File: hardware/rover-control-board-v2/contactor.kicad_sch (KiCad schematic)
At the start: 9 parts, among them Q27 Q_NMOS_DGS

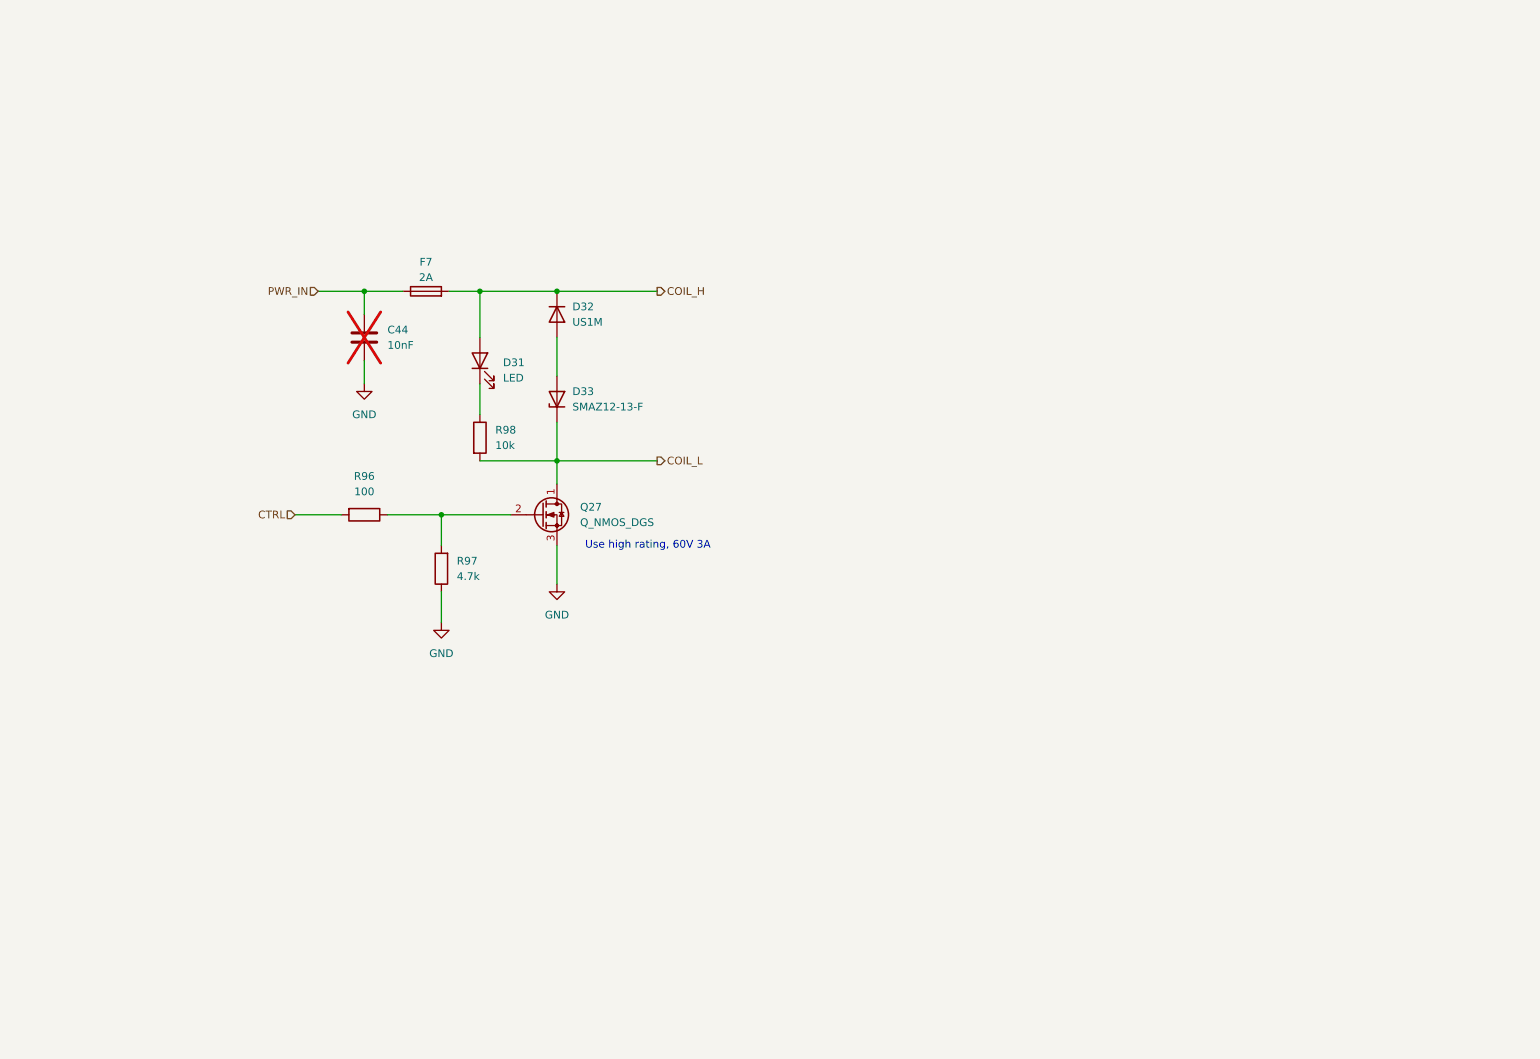
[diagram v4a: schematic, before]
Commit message: footprints and BOM additions
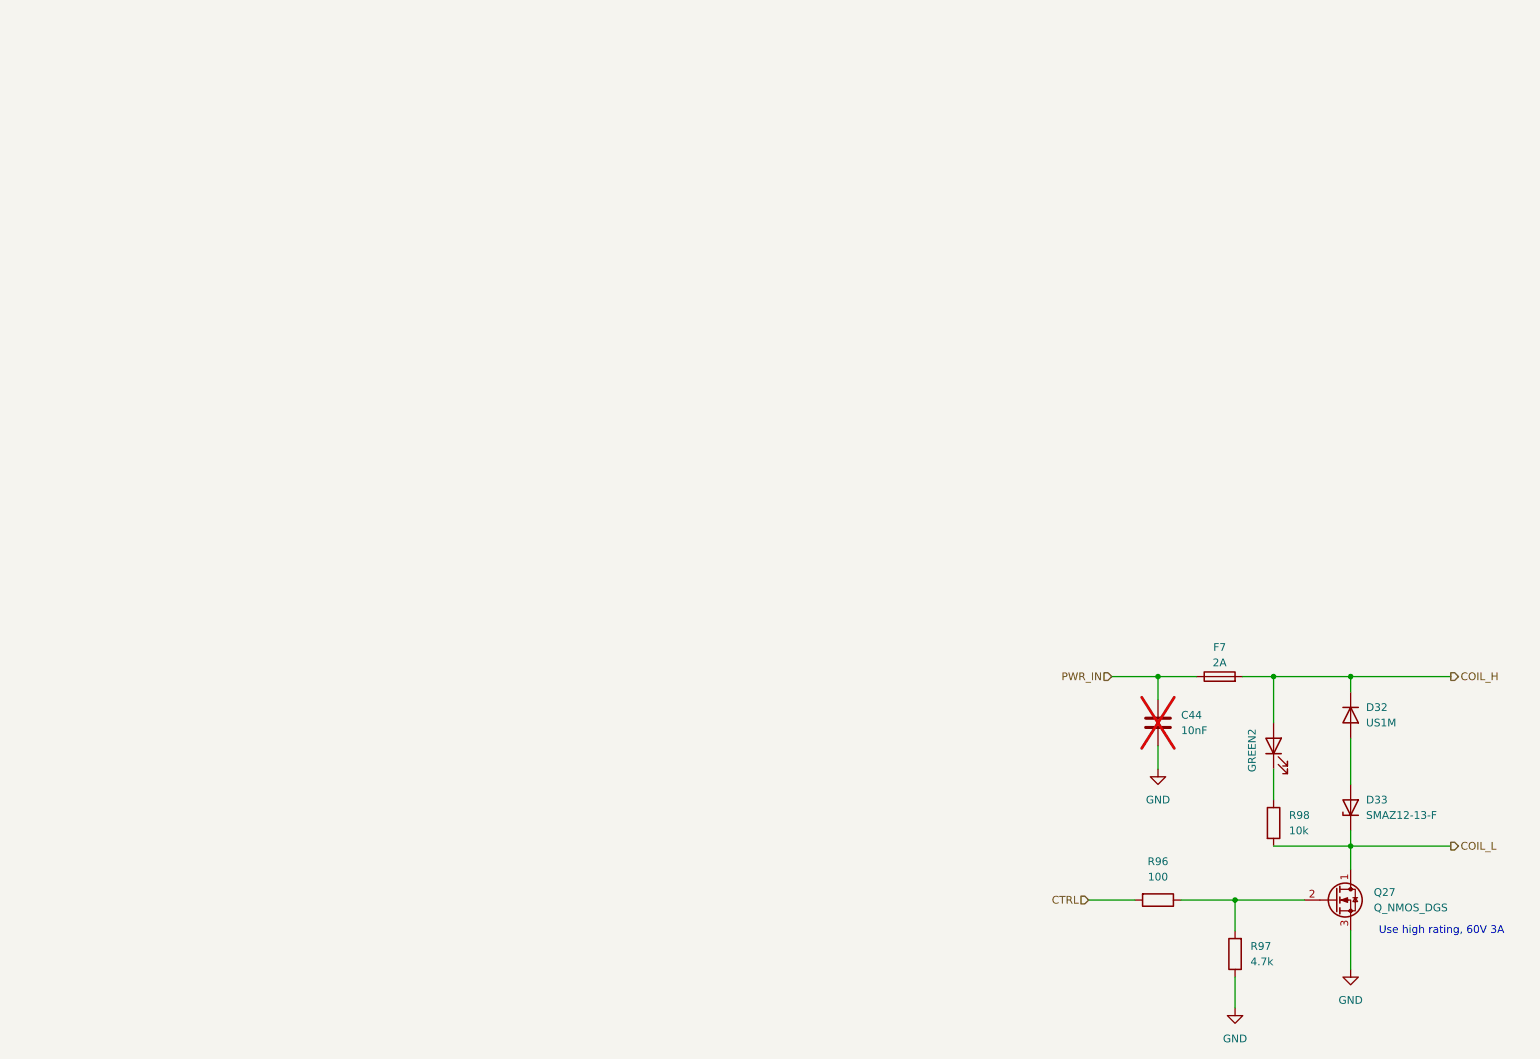
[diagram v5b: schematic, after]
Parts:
- removed D31: LED, symbol Device:LED
- added GREEN2: 350-599, LED_SMD:LED_0805_2012Metric, symbol Device:LED
- C44: footprint (none) -> Capacitor_SMD:C_0603_1608Metric
- D32: digikey_part_num (none) -> 4878-US1MCT-ND
- D33: footprint (none) -> Diode_SMD:D_SMA; digikey_part_num (none) -> SMAZ12-FDICT-ND
- R96, R97, R98: footprint (none) -> Resistor_SMD:R_0603_1608Metric
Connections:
- net COIL_H: now also GREEN2.2 (A)
- net at R98.1: now also GREEN2.1 (K)
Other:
- title: (none) -> Rover Control Board
- moved on the sheet: C44, D32, D33, F7, Q27, R96, R97, R98

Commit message: BOM
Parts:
- removed Q27: Q_NMOS_DGS, symbol Transistor_FET:Q_NMOS_DGS
- added Q3: NMOS_GDS, Package_TO_SOT_SMD:SOT-223, symbol Transistor_FET_Other:Q_NMOS_Depletion_GDS
- F7: footprint (none) -> Fuse:Fuse_2920_7451Metric_Pad2.10x5.45mm_HandSolder; digikey_part_num (none) -> 5923-0ZCF0100AF2ACT-ND
- GREEN2: digikey_part_num (none) -> 350-5991180147FCT-ND
- R96: value 100 -> 100R; digikey_part_num (none) -> 541-100HCT-ND
- R97: digikey_part_num (none) -> 311-4.70KHRCT-ND
- R98: digikey_part_num (none) -> 311-10.0KHRCT-ND
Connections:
- net COIL_L: now also Q3.2 (D)
- net GND: now also Q3.3 (S)
- net at R96.1, R97.2: now also Q3.1 (G)
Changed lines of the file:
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@@
+			)
+		)
+		(property "digikey_part_num" "350-5991180147FCT-ND"
+			(at 207.01 120.65 0)
+			(hide yes)
+			(show_name no)
+			(do_not_autoplace no)
+			(effects
+				(font
+					(size 1.27 1.27)
+				)
 			)
 		)
@@
 	)
 	(symbol
-		(lib_id "Transistor_FET:Q_NMOS_DGS")
+		(lib_id "Transistor_FET_Other:Q_NMOS_Depletion_GDS")
 		(at 217.17 146.05 0)
 		(unit 1)
@@
 		(dnp no)
 		(fields_autoplaced yes)
-		(property "Reference" "Q27"
+		(property "Reference" "Q3"
 			(at 223.52 144.7799 0)
 			(show_name no)
@@
 			)
 		)
-		(property "Value" "Q_NMOS_DGS"
+		(property "Value" "NMOS_GDS"
 			(at 223.52 147.3199 0)
 			(show_name no)
@@
 			)
 		)
-		(property "Footprint" ""
-			(at 222.25 143.51 0)
-			(hide yes)
-			(show_name no)
-			(do_not_autoplace no)
-			(effects
-				(font
-					(size 1.27 1.27)
-				)
-			)
-		)
-		(property "Datasheet" ""
+		(property "Footprint" "Package_TO_SOT_SMD:SOT-223"
 			(at 217.17 146.05 0)
 			(hide yes)
@@
 			)
 		)
-		(property "Description" "N-MOSFET transistor, drain/gate/source"
+		(property "Datasheet" ""
 			(at 217.17 146.05 0)
 			(hide yes)
@@
 			)
 		)
+		(property "Description" "Depletion-mode N-channel MOSFET gate/drain/source"
+			(at 217.17 146.05 0)
+			(hide yes)
+			(show_name no)
+			(do_not_autoplace no)
+			(effects
+				(font
+					(size 1.27 1.27)
+				)
+			)
+		)
+		(property "digikey_part_num" "NTF3055-100T1GOSCT-ND"
+			(at 217.17 146.05 0)
+			(hide yes)
+			(show_name no)
+			(do_not_autoplace no)
+			(effects
+				(font
+					(size 1.27 1.27)
+				)
+			)
+		)
+		(pin "3"
+		)
 		(pin "2"
 		)
 		(pin "1"
 		)
-		(pin "3"
-		)
-		(instances
-			(project "rover-control-board-v2"
-				(path "/ed12625f-743c-4dd1-a6f4-666aeca01e2d/f186a5df-bce3-4173-b0d9-882f1a8a692c"
-					(reference "Q27")
+		(instances
+			(project "rover-control-board-v2"
+				(path "/ed12625f-743c-4dd1-a6f4-666aeca01e2d/f186a5df-bce3-4173-b0d9-882f1a8a692c"
+					(reference "Q3")
 					(unit 1)
 				)
@@
 			)
 		)
-		(property "Value" "100"
+		(property "Value" "100R"
 			(at 187.96 142.24 90)
 			(show_name no)
@@
 		(property "Description" "Resistor"
 			(at 187.96 146.05 0)
+			(hide yes)
+			(show_name no)
+			(do_not_autoplace no)
+			(effects
+				(font
+					(size 1.27 1.27)
+				)
+			)
+		)
+		(property "digikey_part_num" "541-100HCT-ND"
+			(at 187.96 146.05 90)
 			(hide yes)
 			(show_name no)
@@
 			)
 		)
+		(property "digikey_part_num" "311-10.0KHRCT-ND"
+			(at 207.01 133.35 0)
+			(hide yes)
+			(show_name no)
+			(do_not_autoplace no)
+			(effects
+				(font
+					(size 1.27 1.27)
+				)
+			)
+		)
 		(pin "2"
 		)
@@
 			)
 		)
-		(property "Footprint" ""
+		(property "Footprint" "Fuse:Fuse_2920_7451Metric_Pad2.10x5.45mm_HandSolder"
 			(at 198.12 110.998 90)
 			(hide yes)
@@
 		(property "Description" "Fuse"
 			(at 198.12 109.22 0)
+			(hide yes)
+			(show_name no)
+			(do_not_autoplace no)
+			(effects
+				(font
+					(size 1.27 1.27)
+				)
+			)
+		)
+		(property "digikey_part_num" "5923-0ZCF0100AF2ACT-ND"
+			(at 198.12 109.22 90)
 			(hide yes)
 			(show_name no)
@@
 			(at 200.66 154.94 0)
 			(hide yes)
+			(show_name no)
+			(do_not_autoplace no)
+			(effects
+				(font
+					(size 1.27 1.27)
+				)
+			)
+		)
+		(property "digikey_part_num" "311-4.70KHRCT-ND"
+			(at 200.66 154.94 0)
+			(hide yes)
